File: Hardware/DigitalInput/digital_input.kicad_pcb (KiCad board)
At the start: 4 copper layers, 70 x 59 mm, 2 parts, among them CN10 Conn_02x19_Odd_Even, CN7 Conn_02x19_Odd_Even

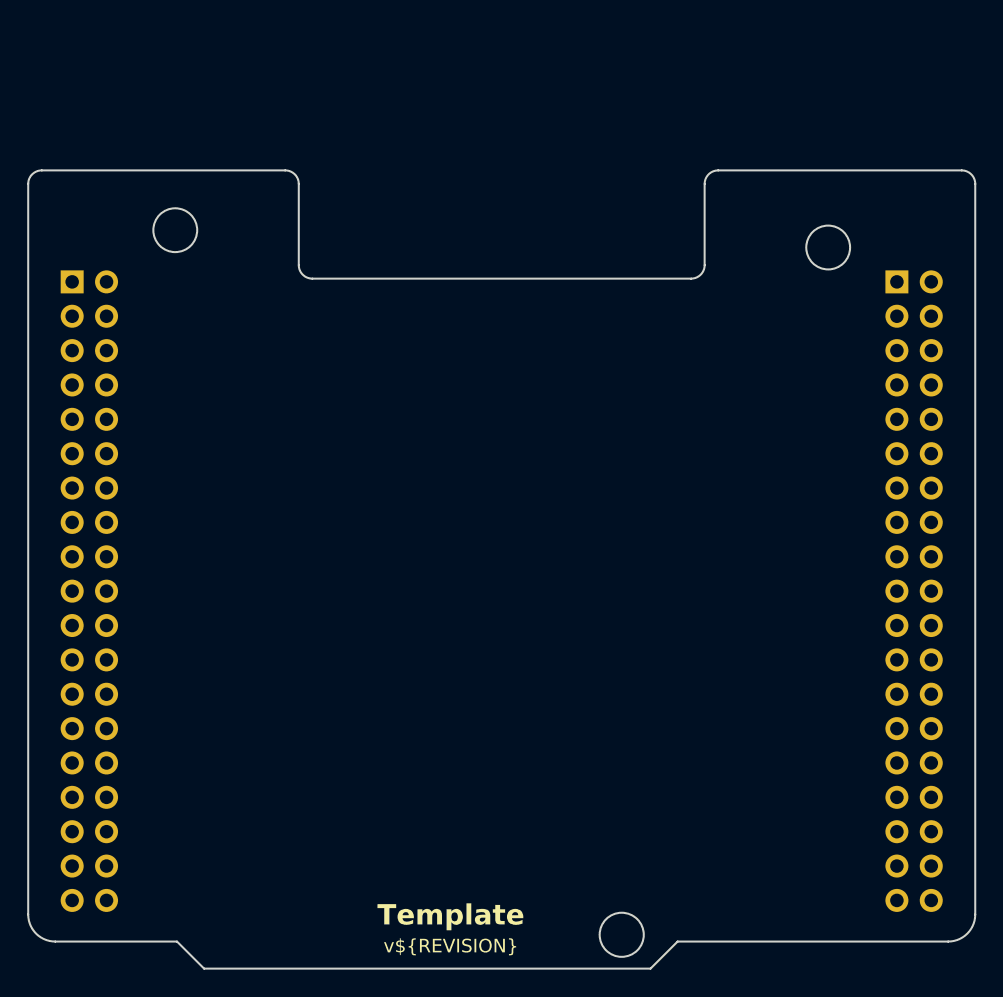
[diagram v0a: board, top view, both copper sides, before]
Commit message: digital output & digital input update
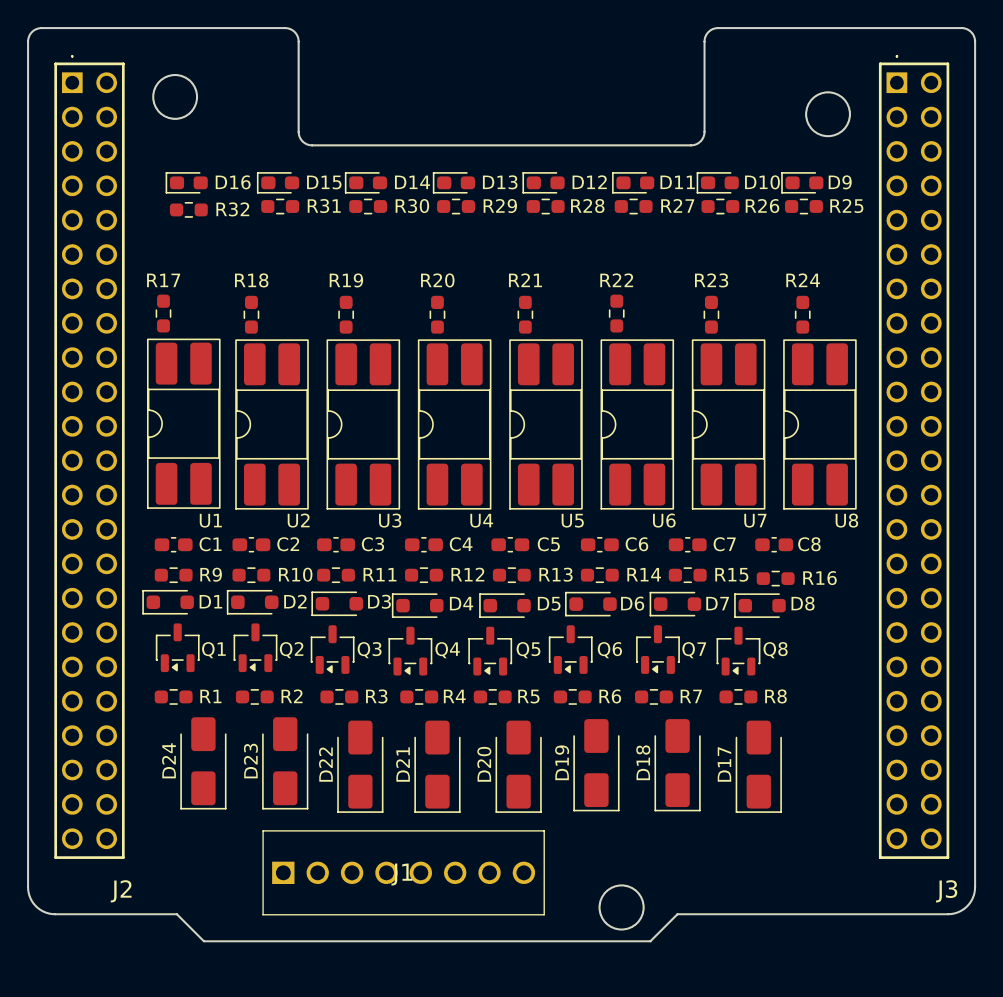
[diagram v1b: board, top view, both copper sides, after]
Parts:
- removed CN10, CN7: Conn_02x19_Odd_Even, Connector_PinSocket_2.54mm:PinSocket_2x19_P2.54mm_Vertical
- added C1: 1n, Capacitor_SMD:C_0603_1608Metric_Pad1.08x0.95mm_HandSolder, F.Cu at (126.8, 86.8)
- added C2: 1n, Capacitor_SMD:C_0603_1608Metric_Pad1.08x0.95mm_HandSolder, F.Cu at (132.5, 86.8)
- added C3: 1n, Capacitor_SMD:C_0603_1608Metric_Pad1.08x0.95mm_HandSolder, F.Cu at (138.8, 86.8)
- added C4: 1n, Capacitor_SMD:C_0603_1608Metric_Pad1.08x0.95mm_HandSolder, F.Cu at (145.2, 86.8)
- added C5: 1n, Capacitor_SMD:C_0603_1608Metric_Pad1.08x0.95mm_HandSolder, F.Cu at (151.6, 86.8)
- added C6: 1n, Capacitor_SMD:C_0603_1608Metric_Pad1.08x0.95mm_HandSolder, F.Cu at (158.2, 86.8)
- added C7: 1n, Capacitor_SMD:C_0603_1608Metric_Pad1.08x0.95mm_HandSolder, F.Cu at (164.8, 86.8)
- added C8: 1n, Capacitor_SMD:C_0603_1608Metric_Pad1.08x0.95mm_HandSolder, F.Cu at (171.1, 86.8)
- added D1: BZX384-B9V1, Diode_SMD:D_SOD-323_HandSoldering, F.Cu at (126.5, 91.0)
- added D10: LD_DI1, LED_SMD:LED_0603_1608Metric_Pad1.05x0.95mm_HandSolder, F.Cu at (167.1, 60.0)
- added D11: LD_DI2, LED_SMD:LED_0603_1608Metric_Pad1.05x0.95mm_HandSolder, F.Cu at (160.9, 60.0)
- added D12: LD_DI3, LED_SMD:LED_0603_1608Metric_Pad1.05x0.95mm_HandSolder, F.Cu at (154.2, 60.0)
- added D13: LD_DI4, LED_SMD:LED_0603_1608Metric_Pad1.05x0.95mm_HandSolder, F.Cu at (147.6, 60.0)
- added D14: LD_DI5, LED_SMD:LED_0603_1608Metric_Pad1.05x0.95mm_HandSolder, F.Cu at (141.1, 60.0)
- added D15: LD_DI6, LED_SMD:LED_0603_1608Metric_Pad1.05x0.95mm_HandSolder, F.Cu at (134.6, 60.0)
- added D16: LD_DI7, LED_SMD:LED_0603_1608Metric_Pad1.05x0.95mm_HandSolder, F.Cu at (127.9, 60.0)
- added D17: SMA6L28A, Diode_SMD:D_SMA, F.Cu at (170.0, 103.0)
- added D18: SMA6L28A, Diode_SMD:D_SMA, F.Cu at (164.0, 102.9)
- added D19: SMA6L28A, Diode_SMD:D_SMA, F.Cu at (158.0, 102.9)
- added D2: BZX384-B9V1, Diode_SMD:D_SOD-323_HandSoldering, F.Cu at (132.8, 91.0)
- added D20: SMA6L28A, Diode_SMD:D_SMA, F.Cu at (152.2, 103.0)
- added D21: SMA6L28A, Diode_SMD:D_SMA, F.Cu at (146.2, 103.0)
- added D22: SMA6L28A, Diode_SMD:D_SMA, F.Cu at (140.6, 103.0)
- added D23: SMA6L28A, Diode_SMD:D_SMA, F.Cu at (135.0, 102.8)
- added D24: SMA6L28A, Diode_SMD:D_SMA, F.Cu at (128.9, 102.8)
- added D3: BZX384-B9V1, Diode_SMD:D_SOD-323_HandSoldering, F.Cu at (139.0, 91.1)
- added D4: BZX384-B9V1, Diode_SMD:D_SOD-323_HandSoldering, F.Cu at (144.9, 91.2)
- added D5: BZX384-B9V1, Diode_SMD:D_SOD-323_HandSoldering, F.Cu at (151.4, 91.2)
- added D6: BZX384-B9V1, Diode_SMD:D_SOD-323_HandSoldering, F.Cu at (157.8, 91.1)
- added D7: BZX384-B9V1, Diode_SMD:D_SOD-323_HandSoldering, F.Cu at (164.0, 91.1)
- added D8: BZX384-B9V1, Diode_SMD:D_SOD-323_HandSoldering, F.Cu at (170.2, 91.2)
- added D9: LD_DI0, LED_SMD:LED_0603_1608Metric_Pad1.05x0.95mm_HandSolder, F.Cu at (173.4, 60.0)
- added J1: DIGITAL INPUT, PLC_STM:1725711, F.Cu at (134.9, 111.0)
- added J2: NUCLEO LEFT, PLC_STM:PRT12790, F.Cu at (119.3, 52.6)
- added J3: NUCLEO RIGHT, PLC_STM:PRT12790, F.Cu at (180.2, 52.6)
- added Q1: SI2347DS, Package_TO_SOT_SMD:SOT-23-3, F.Cu at (127.0, 94.4)
- added Q2: SI2347DS, Package_TO_SOT_SMD:SOT-23-3, F.Cu at (132.8, 94.4)
- added Q3: SI2347DS, Package_TO_SOT_SMD:SOT-23-3, F.Cu at (138.5, 94.5)
- added Q4: SI2347DS, Package_TO_SOT_SMD:SOT-23-3, F.Cu at (144.2, 94.6)
- added Q5: SI2347DS, Package_TO_SOT_SMD:SOT-23-3, F.Cu at (150.2, 94.6)
- added Q6: SI2347DS, Package_TO_SOT_SMD:SOT-23-3, F.Cu at (156.1, 94.5)
- added Q7: SI2347DS, Package_TO_SOT_SMD:SOT-23-3, F.Cu at (162.6, 94.5)
- added Q8: SI2347DS, Package_TO_SOT_SMD:SOT-23-3, F.Cu at (168.5, 94.6)
- added R1: 47k, Resistor_SMD:R_0603_1608Metric_Pad0.98x0.95mm_HandSolder, F.Cu at (126.8, 98.0)
- added R10: 1k, Resistor_SMD:R_0603_1608Metric_Pad0.98x0.95mm_HandSolder, F.Cu at (132.5, 89.0)
- added R11: 1k, Resistor_SMD:R_0603_1608Metric_Pad0.98x0.95mm_HandSolder, F.Cu at (138.8, 89.0)
- added R12: 1k, Resistor_SMD:R_0603_1608Metric_Pad0.98x0.95mm_HandSolder, F.Cu at (145.2, 89.0)
- added R13: 1k, Resistor_SMD:R_0603_1608Metric_Pad0.98x0.95mm_HandSolder, F.Cu at (151.8, 89.0)
- added R14: 1k, Resistor_SMD:R_0603_1608Metric_Pad0.98x0.95mm_HandSolder, F.Cu at (158.2, 89.0)
- added R15: 1k, Resistor_SMD:R_0603_1608Metric_Pad0.98x0.95mm_HandSolder, F.Cu at (164.8, 89.0)
- added R16: 1k, Resistor_SMD:R_0603_1608Metric_Pad0.98x0.95mm_HandSolder, F.Cu at (171.2, 89.2)
- added R17: 1k, Resistor_SMD:R_0603_1608Metric_Pad0.98x0.95mm_HandSolder, F.Cu at (126.0, 69.7)
- added R18: 1k, Resistor_SMD:R_0603_1608Metric_Pad0.98x0.95mm_HandSolder, F.Cu at (132.5, 69.8)
- added R19: 1k, Resistor_SMD:R_0603_1608Metric_Pad0.98x0.95mm_HandSolder, F.Cu at (139.5, 69.8)
- added R2: 47k, Resistor_SMD:R_0603_1608Metric_Pad0.98x0.95mm_HandSolder, F.Cu at (132.8, 98.0)
- added R20: 1k, Resistor_SMD:R_0603_1608Metric_Pad0.98x0.95mm_HandSolder, F.Cu at (146.2, 69.8)
- added R21: 1k, Resistor_SMD:R_0603_1608Metric_Pad0.98x0.95mm_HandSolder, F.Cu at (152.8, 69.8)
- added R22: 1k, Resistor_SMD:R_0603_1608Metric_Pad0.98x0.95mm_HandSolder, F.Cu at (159.5, 69.7)
- added R23: 1k, Resistor_SMD:R_0603_1608Metric_Pad0.98x0.95mm_HandSolder, F.Cu at (166.5, 69.8)
- added R24: 1k, Resistor_SMD:R_0603_1608Metric_Pad0.98x0.95mm_HandSolder, F.Cu at (173.2, 69.8)
- added R25: 220R, Resistor_SMD:R_0603_1608Metric_Pad0.98x0.95mm_HandSolder, F.Cu at (173.3, 61.8)
- added R26: 220R, Resistor_SMD:R_0603_1608Metric_Pad0.98x0.95mm_HandSolder, F.Cu at (167.2, 61.8)
- added R27: 220R, Resistor_SMD:R_0603_1608Metric_Pad0.98x0.95mm_HandSolder, F.Cu at (160.8, 61.8)
- added R28: 220R, Resistor_SMD:R_0603_1608Metric_Pad0.98x0.95mm_HandSolder, F.Cu at (154.2, 61.8)
- added R29: 220R, Resistor_SMD:R_0603_1608Metric_Pad0.98x0.95mm_HandSolder, F.Cu at (147.6, 61.8)
- added R3: 47k, Resistor_SMD:R_0603_1608Metric_Pad0.98x0.95mm_HandSolder, F.Cu at (139.0, 98.0)
- added R30: 220R, Resistor_SMD:R_0603_1608Metric_Pad0.98x0.95mm_HandSolder, F.Cu at (141.1, 61.8)
- added R31: 220R, Resistor_SMD:R_0603_1608Metric_Pad0.98x0.95mm_HandSolder, F.Cu at (134.6, 61.8)
- added R32: 220R, Resistor_SMD:R_0603_1608Metric_Pad0.98x0.95mm_HandSolder, F.Cu at (127.9, 62.0)
- added R4: 47k, Resistor_SMD:R_0603_1608Metric_Pad0.98x0.95mm_HandSolder, F.Cu at (144.9, 98.0)
- added R5: 47k, Resistor_SMD:R_0603_1608Metric_Pad0.98x0.95mm_HandSolder, F.Cu at (150.3, 98.0)
- added R6: 47k, Resistor_SMD:R_0603_1608Metric_Pad0.98x0.95mm_HandSolder, F.Cu at (156.2, 98.0)
- added R7: 47k, Resistor_SMD:R_0603_1608Metric_Pad0.98x0.95mm_HandSolder, F.Cu at (162.2, 98.0)
- added R8: 47k, Resistor_SMD:R_0603_1608Metric_Pad0.98x0.95mm_HandSolder, F.Cu at (168.5, 98.0)
- added R9: 1k, Resistor_SMD:R_0603_1608Metric_Pad0.98x0.95mm_HandSolder, F.Cu at (126.8, 89.0)
- added U1: VO615A-3, Package_DIP:DIP-4_W8.89mm_SMDSocket_LongPads, F.Cu at (127.5, 77.8)
- added U2: VO615A-3, Package_DIP:DIP-4_W8.89mm_SMDSocket_LongPads, F.Cu at (134.0, 77.9)
- added U3: VO615A-3, Package_DIP:DIP-4_W8.89mm_SMDSocket_LongPads, F.Cu at (140.8, 77.9)
- added U4: VO615A-3, Package_DIP:DIP-4_W8.89mm_SMDSocket_LongPads, F.Cu at (147.5, 77.9)
- added U5: VO615A-3, Package_DIP:DIP-4_W8.89mm_SMDSocket_LongPads, F.Cu at (154.3, 77.9)
- added U6: VO615A-3, Package_DIP:DIP-4_W8.89mm_SMDSocket_LongPads, F.Cu at (161.0, 77.9)
- added U7: VO615A-3, Package_DIP:DIP-4_W8.89mm_SMDSocket_LongPads, F.Cu at (167.8, 77.9)
- added U8: VO615A-3, Package_DIP:DIP-4_W8.89mm_SMDSocket_LongPads, F.Cu at (174.5, 77.9)
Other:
- board size 70 x 59 mm -> 70 x 67.5 mm
- board text removed: "Template"
- board text removed: "v${REVISION}"
- board text removed: "®©®"

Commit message: digital input finished
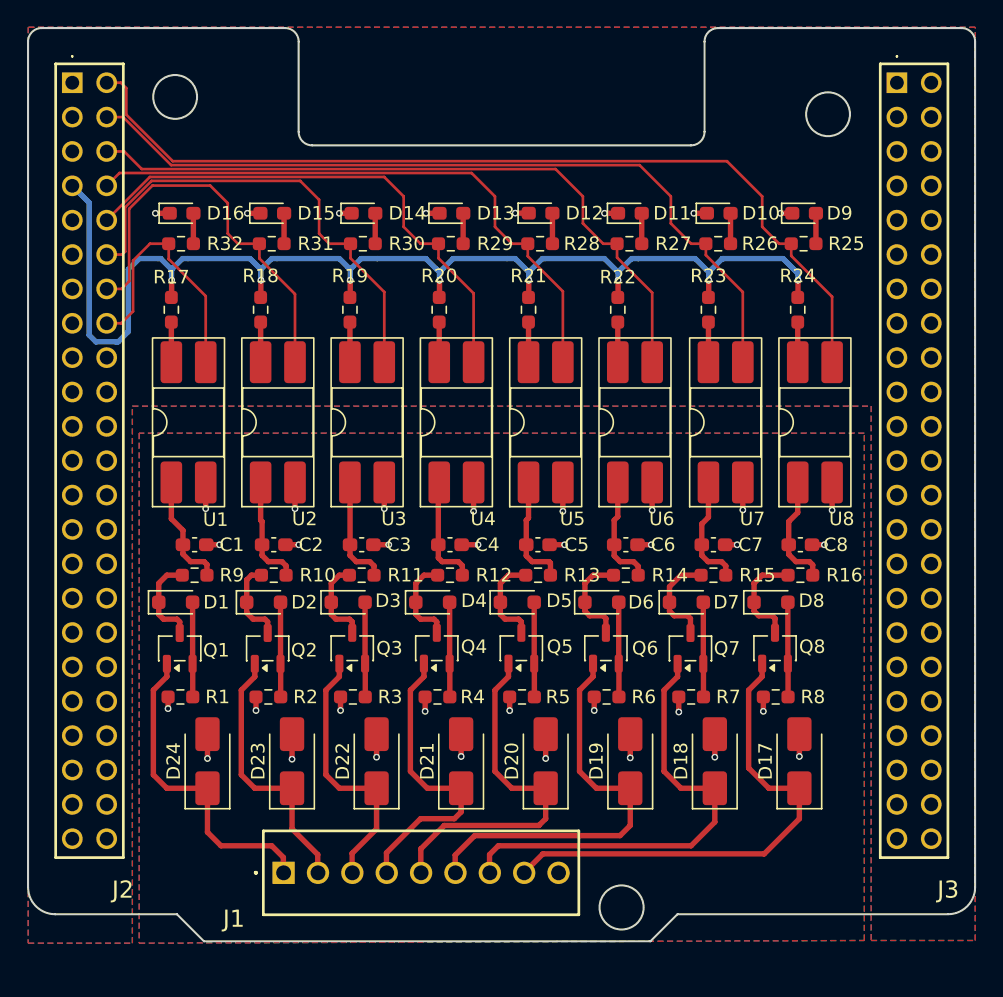
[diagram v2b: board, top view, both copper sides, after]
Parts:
- J1: footprint PLC_STM:1725711 -> PLC_STM:1725724
- moved D17 3.01 mm to (173.0, 102.8)
- moved R31 2.82 mm to (134.0, 64.5)
- moved R28 2.78 mm to (153.8, 64.5)
- moved R29 2.78 mm to (147.2, 64.5)
- moved R30 2.78 mm to (140.7, 64.5)
- moved R27 2.77 mm to (160.4, 64.5)
- moved R26 2.75 mm to (167.0, 64.5)
- moved D18 2.75 mm to (166.8, 102.8)
- moved R25 2.75 mm to (173.3, 64.5)
- moved R7 2.75 mm to (165.0, 98.0)
- moved R8 2.75 mm to (171.2, 98.0)
- moved Q8 2.71 mm to (171.2, 94.4)
- moved Q6 2.60 mm to (158.7, 94.4)
- moved R32 2.57 mm to (127.3, 64.5)
- moved D19 2.50 mm to (160.5, 102.8)
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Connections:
- D17 pad 2: GND -> GNDREF
- D18 pad 2: GND -> GNDREF
- D19 pad 2: GND -> GNDREF
- D20 pad 2: GND -> GNDREF
- D21 pad 2: GND -> GNDREF
- D22 pad 2: GND -> GNDREF
- D23 pad 2: GND -> GNDREF
- D24 pad 2: GND -> GNDREF
- J2 pad 10: unconnected-(J2-Pin_10-Pad10) -> DI_3
- J2 pad 12: unconnected-(J2-Pin_12-Pad12) -> DI_2
- J2 pad 14: unconnected-(J2-Pin_14-Pad14) -> DI_1
- J2 pad 16: unconnected-(J2-Pin_16-Pad16) -> DI_0
- J2 pad 2: unconnected-(J2-Pin_2-Pad2) -> DI_7
- J2 pad 4: unconnected-(J2-Pin_4-Pad4) -> DI_6
- J2 pad 6: unconnected-(J2-Pin_6-Pad6) -> DI_5
- J2 pad 8: unconnected-(J2-Pin_8-Pad8) -> DI_4
- J3 pad 10: AO_1 -> unconnected-(J3-Pin_10-Pad10)
- J3 pad 12: AI_0 -> unconnected-(J3-Pin_12-Pad12)
- J3 pad 13: DI_2 -> unconnected-(J3-Pin_13-Pad13)
- J3 pad 14: AI_1 -> unconnected-(J3-Pin_14-Pad14)
- J3 pad 15: DI_3 -> unconnected-(J3-Pin_15-Pad15)
- J3 pad 17: AO_0 -> unconnected-(J3-Pin_17-Pad17)
- J3 pad 19: DI_4 -> unconnected-(J3-Pin_19-Pad19)
- J3 pad 2: CAN1_RX -> unconnected-(J3-Pin_2-Pad2)
- J3 pad 23: AVDD -> unconnected-(J3-Pin_23-Pad23)
- J3 pad 24: DO_0 -> unconnected-(J3-Pin_24-Pad24)
- J3 pad 25: AGND -> unconnected-(J3-Pin_25-Pad25)
- J3 pad 26: DO_1 -> unconnected-(J3-Pin_26-Pad26)
- J3 pad 28: DO_2 -> unconnected-(J3-Pin_28-Pad28)
- J3 pad 29: DI_5 -> unconnected-(J3-Pin_29-Pad29)
- J3 pad 3: DI_0 -> unconnected-(J3-Pin_3-Pad3)
- J3 pad 30: DO_3 -> unconnected-(J3-Pin_30-Pad30)
- J3 pad 32: DO_4 -> unconnected-(J3-Pin_32-Pad32)
- J3 pad 34: DO_5 -> unconnected-(J3-Pin_34-Pad34)
- J3 pad 35: DI_6 -> unconnected-(J3-Pin_35-Pad35)
- J3 pad 36: DO_6 -> unconnected-(J3-Pin_36-Pad36)
- J3 pad 37: DI_7 -> unconnected-(J3-Pin_37-Pad37)
- J3 pad 38: DO_7 -> unconnected-(J3-Pin_38-Pad38)
- J3 pad 4: CAN1_TX -> unconnected-(J3-Pin_4-Pad4)
- J3 pad 40: UART6_TX -> unconnected-(J3-Pin_40-Pad40)
- J3 pad 42: UART6_RX -> unconnected-(J3-Pin_42-Pad42)
- J3 pad 5: DI_1 -> unconnected-(J3-Pin_5-Pad5)
- J3 pad 6: AVDD -> unconnected-(J3-Pin_6-Pad6)
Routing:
- net +3V3: track 0.00 -> 90.7 mm, vias 0 -> 8
- net DI_7: track 0.00 -> 68.0 mm
- net DI_6: track 0.00 -> 59.2 mm
- net DI_5: track 0.00 -> 51.6 mm
- net GNDREF: track 0.00 -> 46.5 mm, vias 0 -> 32
- net DI_4: track 0.00 -> 44.8 mm
- net DI_3: track 0.00 -> 39.0 mm
- net DI_IN7: track 0.00 -> 36.8 mm
- net DI_2: track 0.00 -> 35.4 mm
- net DI_IN6: track 0.00 -> 34.1 mm
- net DI_IN5: track 0.00 -> 30.6 mm
- net DI_1: track 0.00 -> 30.5 mm
- net DI_IN4: track 0.00 -> 26.8 mm
- net DI_IN0: track 0.00 -> 23.8 mm
- net DI_IN3: track 0.00 -> 22.6 mm
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- added copper zone on B.Cu, net GND
- added copper zone on F.Cu, net GND
- added copper zone on In1.Cu, net GND
- added copper zone on In2.Cu, net GND
- added copper zone on B.Cu, net GNDREF
- added copper zone on F.Cu, net GNDREF
- added copper zone on In1.Cu, net GNDREF
- added copper zone on In2.Cu, net GNDREF

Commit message: digital input pins update
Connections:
- J2 pad 10: DI_3 -> unconnected-(J2-Pin_10-Pad10)
- J2 pad 12: DI_2 -> unconnected-(J2-Pin_12-Pad12)
- J2 pad 14: DI_1 -> DI_4
- J2 pad 16: DI_0 -> unconnected-(J2-Pin_16-Pad16)
- J2 pad 19: unconnected-(J2-Pin_19-Pad19) -> DI_3
- J2 pad 2: DI_7 -> DI_6
- J2 pad 21: unconnected-(J2-Pin_21-Pad21) -> DI_2
- J2 pad 23: unconnected-(J2-Pin_23-Pad23) -> DI_1
- J2 pad 29: unconnected-(J2-Pin_29-Pad29) -> DI_0
- J2 pad 4: DI_6 -> unconnected-(J2-Pin_4-Pad4)
- J2 pad 6: DI_5 -> unconnected-(J2-Pin_6-Pad6)
- J2 pad 8: DI_4 -> DI_5
- J3 pad 18: unconnected-(J3-Pin_18-Pad18) -> DI_7
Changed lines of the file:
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@@
 	(net 65 "unconnected-(J2-Pin_24-Pad24)")
 	(net 66 "unconnected-(J3-Pin_38-Pad38)")
-	(net 67 "unconnected-(J2-Pin_21-Pad21)")
+	(net 67 "unconnected-(J2-Pin_10-Pad10)")
 	(net 68 "unconnected-(J2-Pin_28-Pad28)")
 	(net 69 "unconnected-(J2-Pin_17-Pad17)")
@@
 	(net 72 "unconnected-(J3-Pin_26-Pad26)")
 	(net 73 "unconnected-(J2-Pin_42-Pad42)")
-	(net 74 "unconnected-(J2-Pin_19-Pad19)")
+	(net 74 "unconnected-(J2-Pin_4-Pad4)")
 	(net 75 "unconnected-(J2-Pin_3-Pad3)")
 	(net 76 "unconnected-(J2-Pin_9-Pad9)")
@@
 	(net 92 "unconnected-(J2-Pin_15-Pad15)")
 	(net 93 "unconnected-(J2-Pin_45-Pad45)")
-	(net 94 "unconnected-(J2-Pin_29-Pad29)")
-	(net 95 "unconnected-(J2-Pin_23-Pad23)")
+	(net 94 "unconnected-(J2-Pin_6-Pad6)")
+	(net 95 "unconnected-(J2-Pin_12-Pad12)")
 	(net 96 "unconnected-(J2-Pin_40-Pad40)")
 	(net 97 "unconnected-(J2-Pin_33-Pad33)")
@@
 	(net 106 "unconnected-(J3-Pin_7-Pad7)")
 	(net 107 "unconnected-(J3-Pin_43-Pad43)")
-	(net 108 "unconnected-(J3-Pin_18-Pad18)")
+	(net 108 "unconnected-(J2-Pin_16-Pad16)")
 	(net 109 "unconnected-(J3-Pin_19-Pad19)")
 	(net 110 "unconnected-(J3-Pin_9-Pad9)")
@@
 			(layers "*.Cu" "*.Mask")
 			(remove_unused_layers no)
-			(net 108 "unconnected-(J3-Pin_18-Pad18)")
+			(net 122 "DI_7")
 			(pinfunction "Pin_18")
-			(pintype "passive+no_connect")
+			(pintype "passive")
 		)
 		(pad "19" thru_hole circle
@@
 			(layers "*.Cu" "*.Mask")
 			(remove_unused_layers no)
-			(net 122 "DI_7")
+			(net 119 "DI_6")
 			(pinfunction "Pin_2")
 			(pintype "passive")
@@
 			(layers "*.Cu" "*.Mask")
 			(remove_unused_layers no)
-			(net 119 "DI_6")
+			(net 74 "unconnected-(J2-Pin_4-Pad4)")
 			(pinfunction "Pin_4")
-			(pintype "passive")
+			(pintype "passive+no_connect")
 		)
 		(pad "5" thru_hole circle
@@
 			(layers "*.Cu" "*.Mask")
 			(remove_unused_layers no)
-			(net 116 "DI_5")
+			(net 94 "unconnected-(J2-Pin_6-Pad6)")
 			(pinfunction "Pin_6")
-			(pintype "passive")
+			(pintype "passive+no_connect")
 		)
 		(pad "7" thru_hole circle
@@
 			(layers "*.Cu" "*.Mask")
 			(remove_unused_layers no)
-			(net 112 "DI_4")
+			(net 116 "DI_5")
 			(pinfunction "Pin_8")
 			(pintype "passive")
@@
 			(layers "*.Cu" "*.Mask")
 			(remove_unused_layers no)
-			(net 111 "DI_3")
+			(net 67 "unconnected-(J2-Pin_10-Pad10)")
 			(pinfunction "Pin_10")
-			(pintype "passive")
+			(pintype "passive+no_connect")
 		)
 		(pad "11" thru_hole circle
@@
 			(layers "*.Cu" "*.Mask")
 			(remove_unused_layers no)
-			(net 125 "DI_2")
+			(net 95 "unconnected-(J2-Pin_12-Pad12)")
 			(pinfunction "Pin_12")
-			(pintype "passive")
+			(pintype "passive+no_connect")
 		)
 		(pad "13" thru_hole circle
@@
 			(layers "*.Cu" "*.Mask")
 			(remove_unused_layers no)
-			(net 113 "DI_1")
+			(net 112 "DI_4")
 			(pinfunction "Pin_14")
 			(pintype "passive")
@@
 			(layers "*.Cu" "*.Mask")
 			(remove_unused_layers no)
-			(net 117 "DI_0")
+			(net 108 "unconnected-(J2-Pin_16-Pad16)")
 			(pinfunction "Pin_16")
-			(pintype "passive")
+			(pintype "passive+no_connect")
 		)
 		(pad "17" thru_hole circle
@@
 			(layers "*.Cu" "*.Mask")
 			(remove_unused_layers no)
-			(net 74 "unconnected-(J2-Pin_19-Pad19)")
+			(net 111 "DI_3")
 			(pinfunction "Pin_19")
-			(pintype "passive+no_connect")
+			(pintype "passive")
 		)
 		(pad "20" thru_hole circle
@@
 			(layers "*.Cu" "*.Mask")
 			(remove_unused_layers no)
-			(net 67 "unconnected-(J2-Pin_21-Pad21)")
+			(net 125 "DI_2")
 			(pinfunction "Pin_21")
-			(pintype "passive+no_connect")
+			(pintype "passive")
 		)
 		(pad "22" thru_hole circle
@@
 			(layers "*.Cu" "*.Mask")
 			(remove_unused_layers no)
-			(net 95 "unconnected-(J2-Pin_23-Pad23)")
+			(net 113 "DI_1")
 			(pinfunction "Pin_23")
-			(pintype "passive+no_connect")
+			(pintype "passive")
 		)
 		(pad "24" thru_hole circle
@@
 			(layers "*.Cu" "*.Mask")
 			(remove_unused_layers no)
-			(net 94 "unconnected-(J2-Pin_29-Pad29)")
+			(net 117 "DI_0")
 			(pinfunction "Pin_29")
-			(pintype "passive+no_connect")
+			(pintype "passive")
 		)
 		(pad "30" thru_hole circle

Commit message: digital output & power finished
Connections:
- J2 pad 11: GND -> unconnected-(J2-Pin_11-Pad11)
- J2 pad 13: GND -> unconnected-(J2-Pin_13-Pad13)
- J2 pad 14: DI_4 -> unconnected-(J2-Pin_14-Pad14)
- J2 pad 19: DI_3 -> GND
- J2 pad 2: DI_6 -> unconnected-(J2-Pin_2-Pad2)
- J2 pad 20: unconnected-(J2-Pin_20-Pad20) -> GND
- J2 pad 21: DI_2 -> unconnected-(J2-Pin_21-Pad21)
- J2 pad 22: unconnected-(J2-Pin_22-Pad22) -> GND
- J2 pad 23: DI_1 -> unconnected-(J2-Pin_23-Pad23)
- J2 pad 25: unconnected-(J2-Pin_25-Pad25) -> +3V3
- J2 pad 29: DI_0 -> unconnected-(J2-Pin_29-Pad29)
- J2 pad 30: GND -> unconnected-(J2-Pin_30-Pad30)
- J2 pad 35: unconnected-(J2-Pin_35-Pad35) -> DI_1
- J2 pad 36: unconnected-(J2-Pin_36-Pad36) -> DI_0
- J2 pad 37: unconnected-(J2-Pin_37-Pad37) -> DI_3
- J2 pad 38: unconnected-(J2-Pin_38-Pad38) -> DI_2
- J2 pad 39: GND -> unconnected-(J2-Pin_39-Pad39)
- J2 pad 7: +3V3 -> unconnected-(J2-Pin_7-Pad7)
- J2 pad 8: DI_5 -> GND
- J3 pad 18: DI_7 -> unconnected-(J3-Pin_18-Pad18)
- J3 pad 2: unconnected-(J3-Pin_2-Pad2) -> DI_4
- J3 pad 20: unconnected-(J3-Pin_20-Pad20) -> GND
- J3 pad 22: unconnected-(J3-Pin_22-Pad22) -> DI_7
- J3 pad 27: GND -> unconnected-(J3-Pin_27-Pad27)
- J3 pad 39: GND -> unconnected-(J3-Pin_39-Pad39)
- J3 pad 4: unconnected-(J3-Pin_4-Pad4) -> DI_5
- J3 pad 6: unconnected-(J3-Pin_6-Pad6) -> DI_6
- J3 pad 8: GND -> unconnected-(J3-Pin_8-Pad8)
- J3 pad 9: unconnected-(J3-Pin_9-Pad9) -> GND
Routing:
- net DI_7: track 68.0 -> 20.5 mm
- net DI_3: track 39.0 -> 82.6 mm
- net DI_2: track 35.4 -> 76.9 mm
- net DI_0: track 19.1 -> 47.6 mm
- net DI_1: track 30.5 -> 58.9 mm
- net DI_6: track 59.2 -> 30.9 mm
- net DI_5: track 51.6 -> 38.5 mm
- net DI_4: track 44.8 -> 45.8 mm
